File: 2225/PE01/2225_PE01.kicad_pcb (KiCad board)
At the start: 2 copper layers, 200 x 60 mm, 95 parts

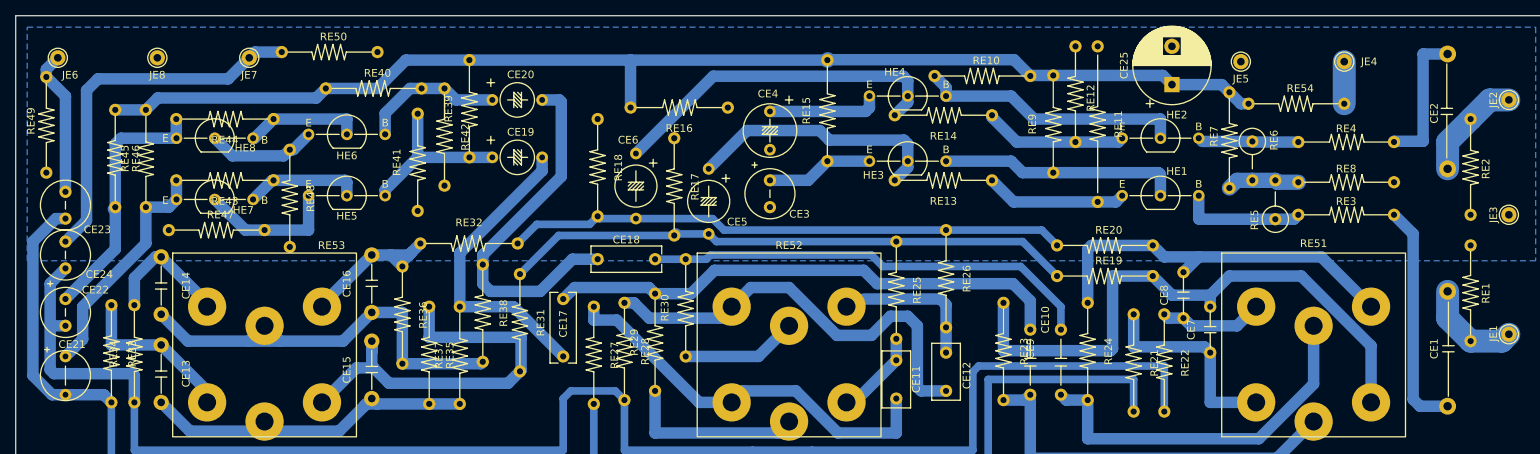
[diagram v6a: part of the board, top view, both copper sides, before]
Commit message: Made more PCB footprints to match schematic symbols. Also aligned component text in PCB silkscreen.
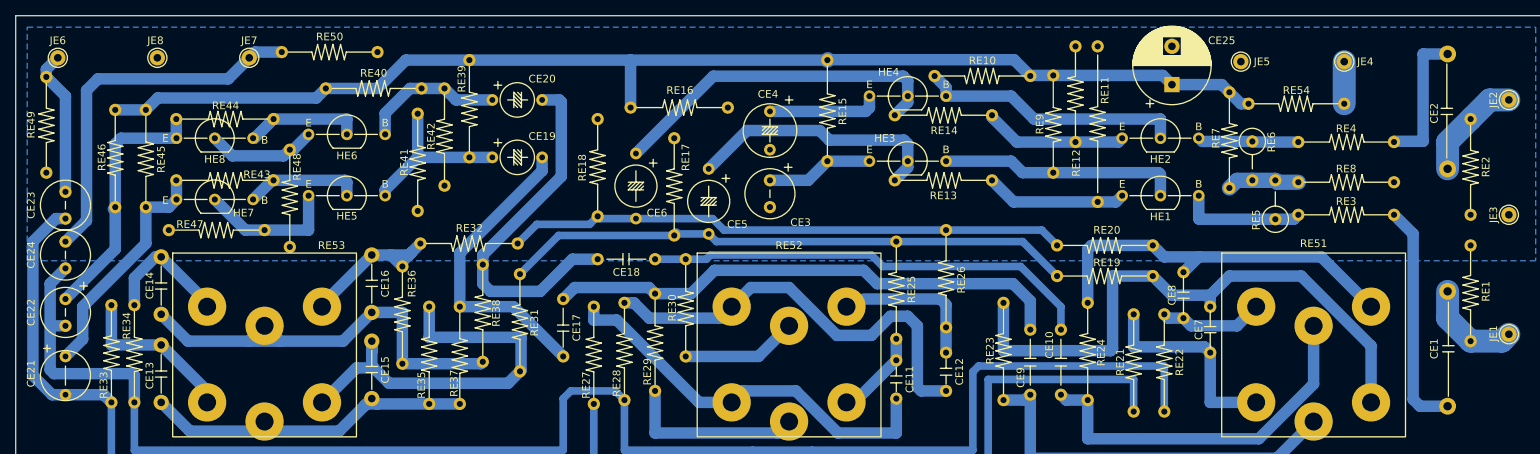
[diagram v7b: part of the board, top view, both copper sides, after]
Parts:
- CE11, CE12: footprint Capacitor_THT:C_Rect_L7.2mm_W3.5mm_P5.00mm_FKS2_FKP2_MKS2_MKP2 -> Capacitor_THT:C_US_Rect_L7.2mm_W3.5mm_P5.00mm_FKS2_FKP2_MKS2_MKP2
- CE17, CE18: footprint Capacitor_THT:C_Rect_L9.0mm_W3.2mm_P7.50mm_MKT -> Capacitor_THT:C_US_Rect_L9.0mm_W3.2mm_P7.50mm_MKT
